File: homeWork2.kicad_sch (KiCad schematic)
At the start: 44 parts, among them J1 Barrel_Jack_Switch_SMT, U1 LM7805_TO220

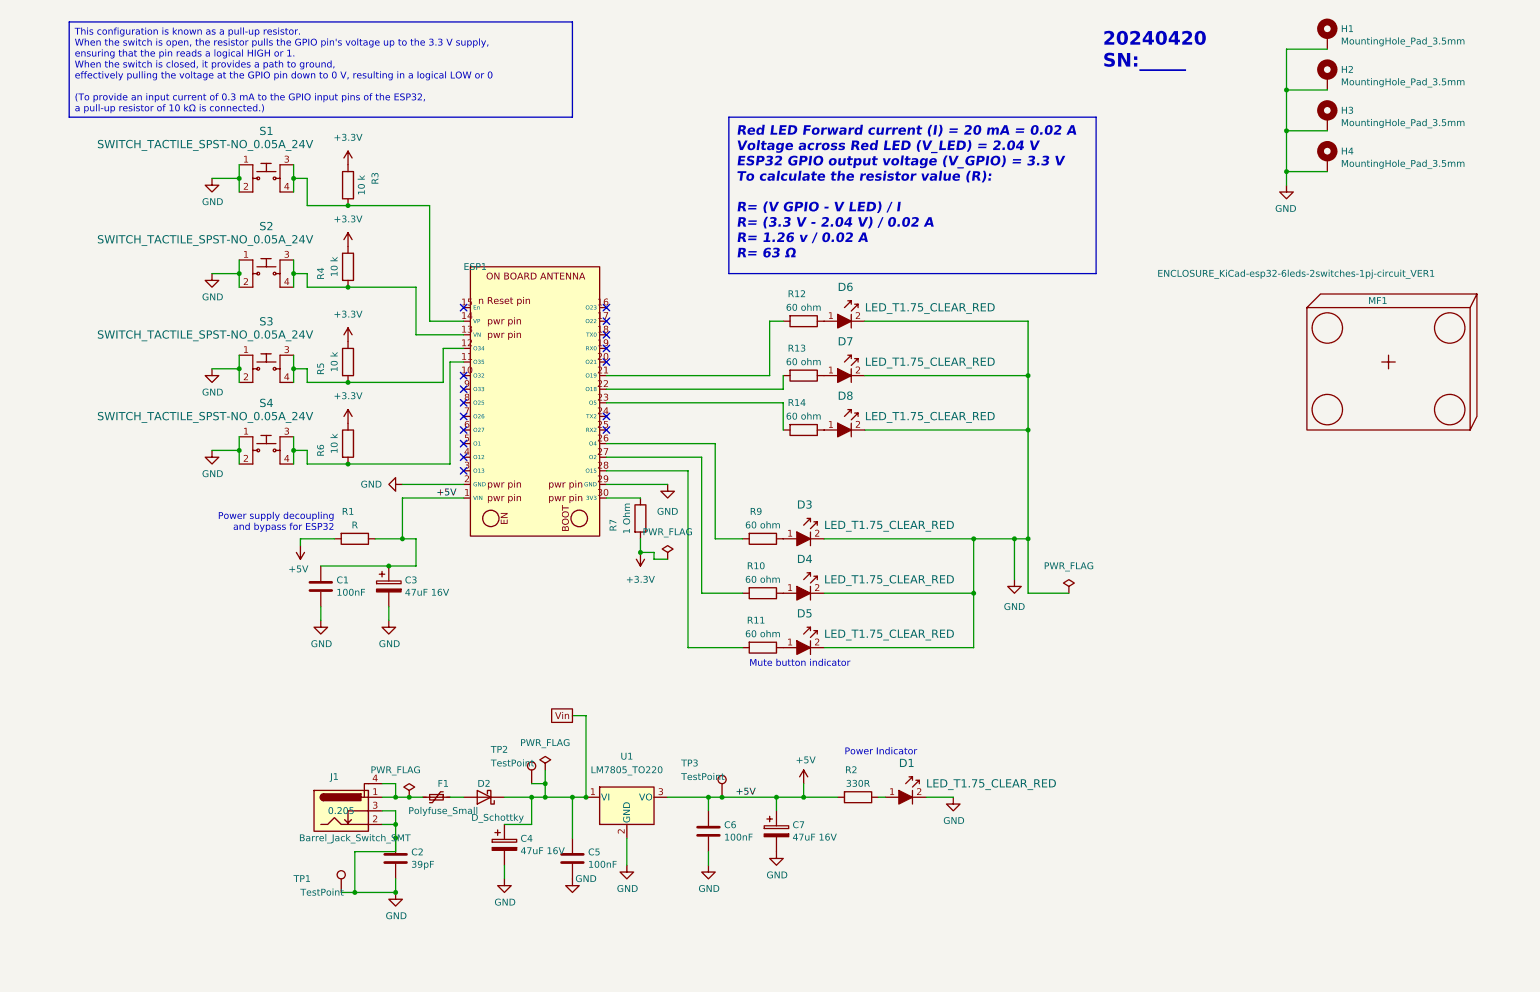
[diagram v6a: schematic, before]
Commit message: Functions have been added to the switches and LEDs, and silkscreen has been included on the PCB to indicate these functions.
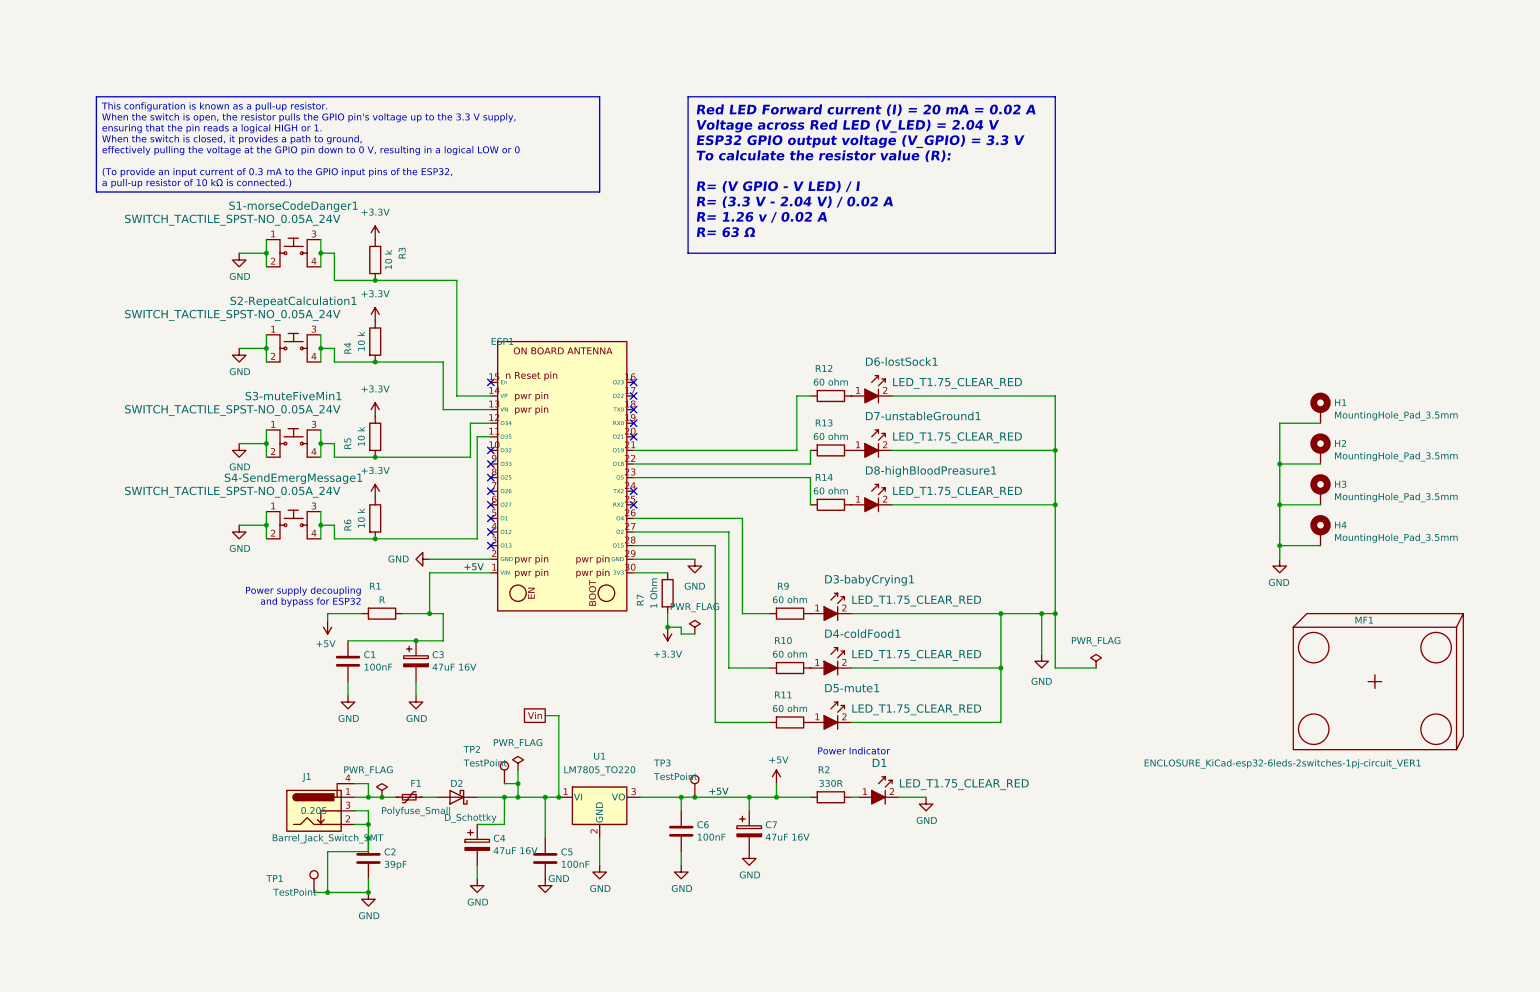
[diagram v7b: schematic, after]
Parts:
- renumbered D3 to D3-babyCrying1, D4 to D4-coldFood1, D5 to D5-mute1, D6 to D6-lostSock1, D7 to D7-unstableGround1, D8 to D8-highBloodPreasure1, S1 to S1-morseCodeDanger1, S2 to S2-RepeatCalculation1, S3 to S3-muteFiveMin1, S4 to S4-SendEmergMessage1
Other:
- note removed: "20240420 SN:_____"
- note removed: "Mute button indicator"
- moved on the sheet: C1, C2, C3, C4, C5, C6, C7, D1, D2, D3-babyCrying1, D4-coldFood1, D5-mute1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

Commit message: Gerber files and enhancements file are added,
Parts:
- R1: value R -> 1R; Cost 0.0015 -> 0.0020
- R7: value 1 Ohm -> 1R
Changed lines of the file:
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@@
       (effects (font (size 1.27 1.27)))
     )
-    (property "Value" "1 Ohm" (at 129.54 120.65 90)
+    (property "Value" "1R" (at 129.54 120.65 90)
       (effects (font (size 1.27 1.27)))
     )
@@
       (effects (font (size 1.27 1.27)))
     )
-    (property "Value" "R" (at 78.74 121.92 90)
+    (property "Value" "1R" (at 78.74 121.92 90)
       (effects (font (size 1.27 1.27)))
     )
@@
       (effects (font (size 1.27 1.27)) hide)
     )
-    (property "Datasheet" "~" (at 78.74 124.46 0)
+    (property "Datasheet" "https://wmsc.lcsc.com/wmsc/upload/file/pdf/v2/lcsc/2304140030_TyoHM-RMC060315-N_C269434.pdf" (at 78.74 124.46 0)
       (effects (font (size 1.27 1.27)) hide)
     )
@@
       (effects (font (size 1.27 1.27)) hide)
     )
-    (property "Cost" "0.0015" (at 78.74 124.46 0)
-      (effects (font (size 1.27 1.27)) hide)
-    )
+    (property "Cost" "0.0020" (at 78.74 124.46 0)
+      (effects (font (size 1.27 1.27)) hide)
+    )
